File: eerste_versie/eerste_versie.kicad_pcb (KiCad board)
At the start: 2 copper layers, 42.5 x 33.7 mm, 21 parts, among them J1 105017-1001, U1 ESP32-WROOM-32U, U2 AMS1117-3.3

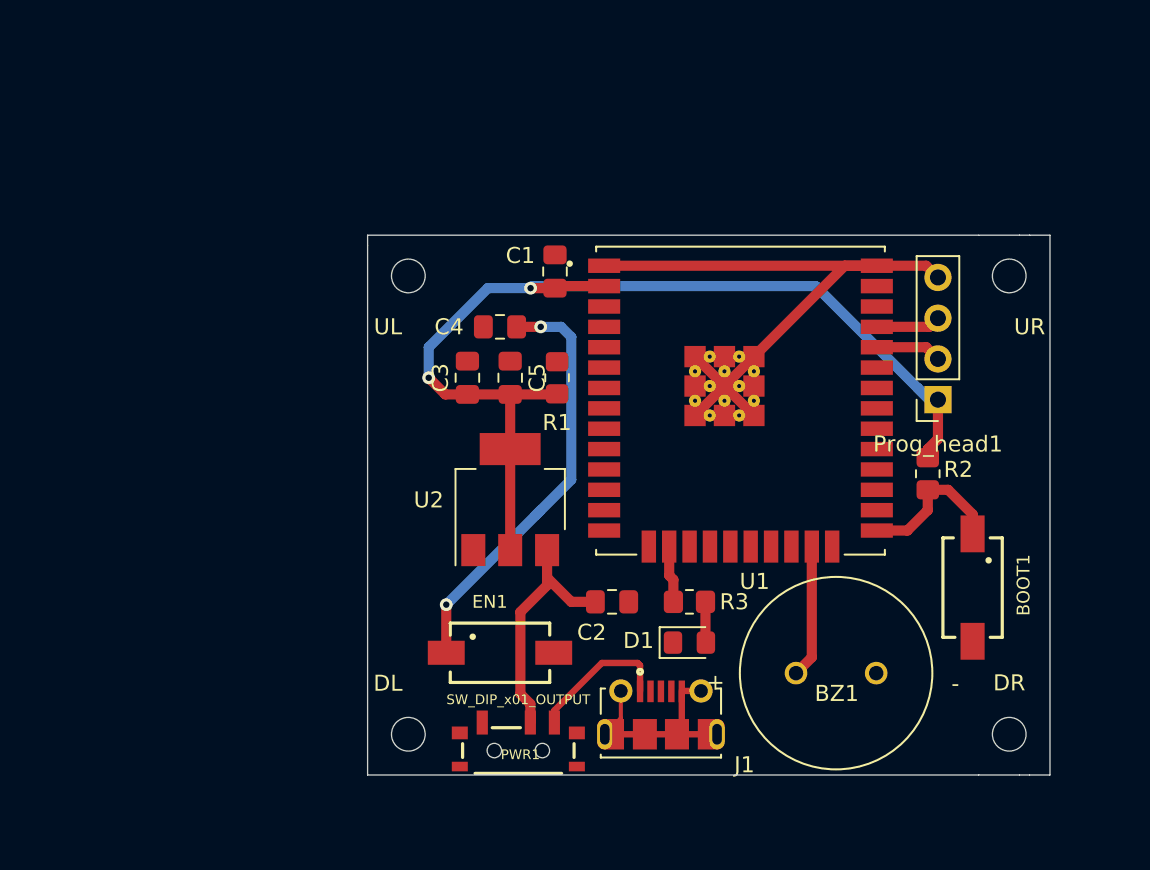
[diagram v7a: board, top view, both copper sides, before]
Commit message: batterij toevoeging
- printkroonsteentje voor aansluiting van batterijkabels toegevoegd
- pull-up weerstand aan IO5 toegevoegd
-3D modellen toegevoegd
- silkscreens in orde gebracht
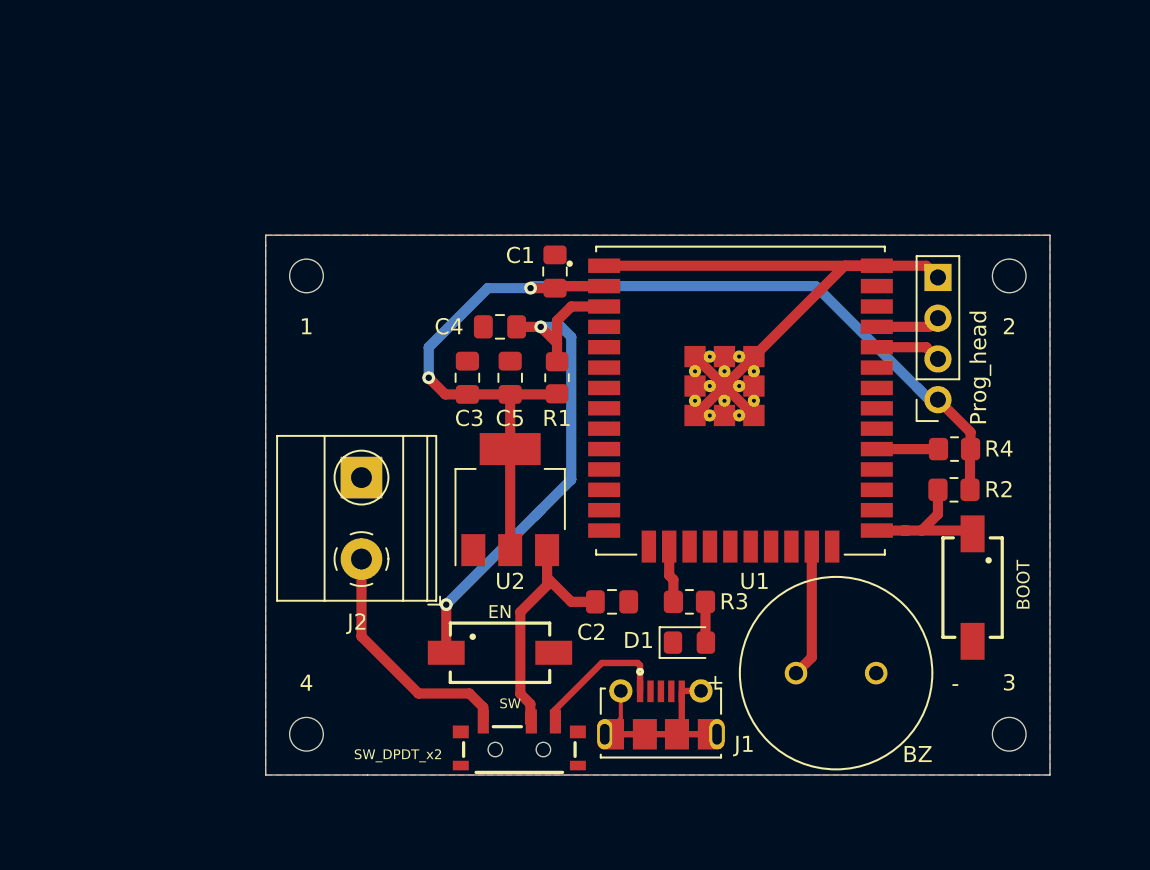
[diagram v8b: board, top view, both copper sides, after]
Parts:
- removed PWR1: SW_DIP_x01_OUTPUT, sparkfun:SWITCH_SPST_SMD_A
- added G***: LOGO, logo:biohazard_symbool, B.Cu at (138.4, 120.7)
- added J2: Conn_01x02, TerminalBlock_Phoenix:TerminalBlock_Phoenix_MKDS-1,5-2-5.08_1x02_P5.08mm_Horizontal, F.Cu at (116.5, 125.0)
- added R4: 10k, Resistor_SMD:R_0805_2012Metric_Pad1.20x1.40mm_HandSolder, F.Cu at (153.4, 118.1)
- added SW: SW_DPDT_x2, sparkfun:SWITCH_SPST_SMD_A, F.Cu at (126.3, 136.8)
- moved 1 6.35 mm to (113.0, 107.3)
- moved 4 6.35 mm to (113.0, 135.9)
- moved R2 1.92 mm to (153.4, 120.7), turned to 180 degrees
- renumbered UL to 1, UR to 2, DR to 3, DL to 4, BOOT1 to BOOT, BZ1 to BZ, EN1 to EN, Prog_head1 to Prog_head
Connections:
- J1 pad 1: Net-(J1-Pad1) -> USB_PWR
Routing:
- net BAT_PWR: track 0.00 -> 15.1 mm
- net USB_PWR: track 0.00 -> 9.00 mm
- net Net-(J1-Pad1): track 9.00 -> 0.00 mm
- net Net-(C4-Pad1): track 26.8 -> 34.1 mm
- net Net-(R4-Pad2): track 0.00 -> 3.84 mm
- net VDD33: track 65.5 -> 68.1 mm
- added copper zone on F.Cu, net GND
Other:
- board size 42.5 x 33.7 mm -> 48.9 x 33.7 mm
- board text added: "1.5m"
- board text added: "BAT PWR"
- board text added: "David Hemeryck Nathan Slembrouck"
- board text added: "GND"
- board text added: "RX"
- board text added: "TX"
- board text added: "USB PWR"
- board text added: "VDD"
